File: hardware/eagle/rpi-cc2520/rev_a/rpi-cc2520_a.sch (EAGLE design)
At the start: 11 parts, among them J1 PINHD-2X12/SMD, J2 PINHD-2X12/SMD

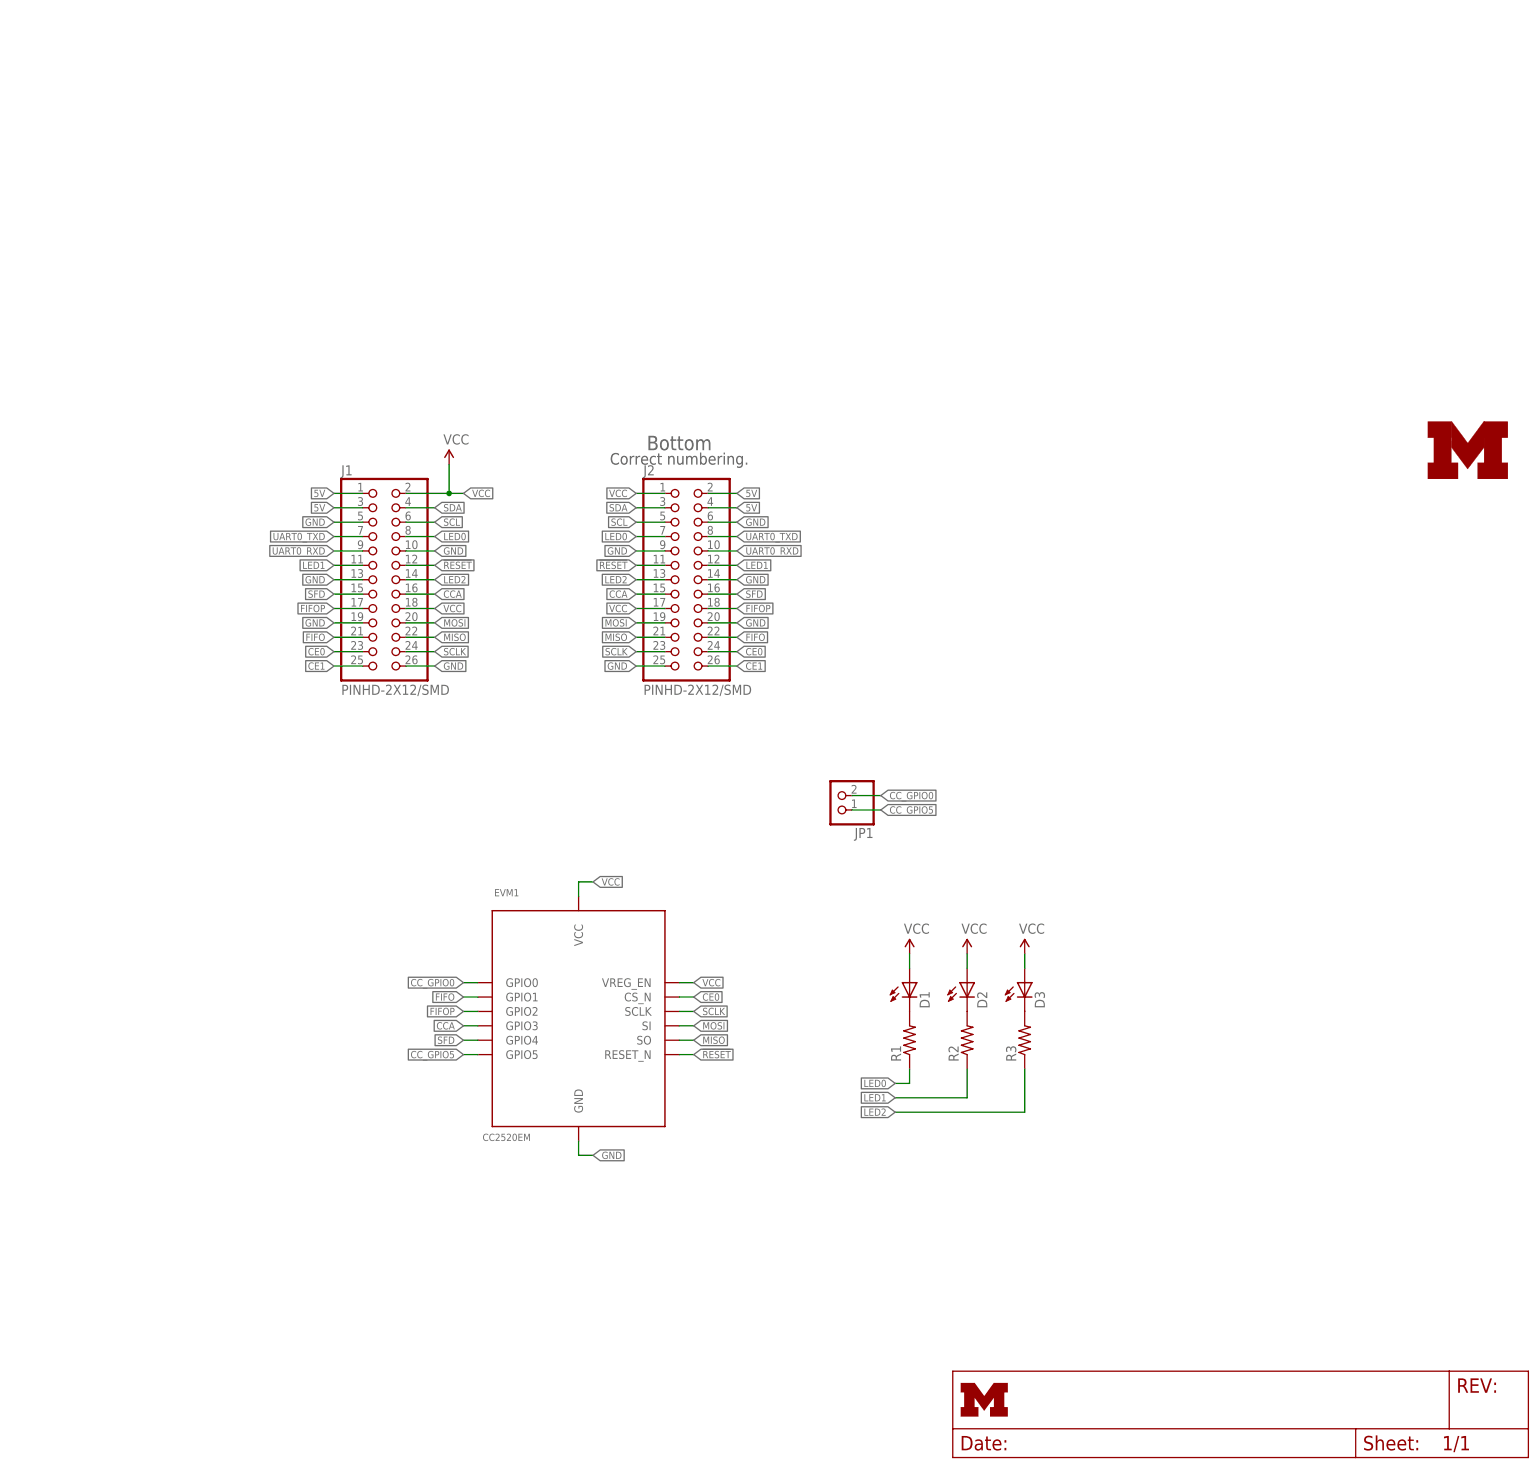
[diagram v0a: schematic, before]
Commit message: adding cc2520 and related parts
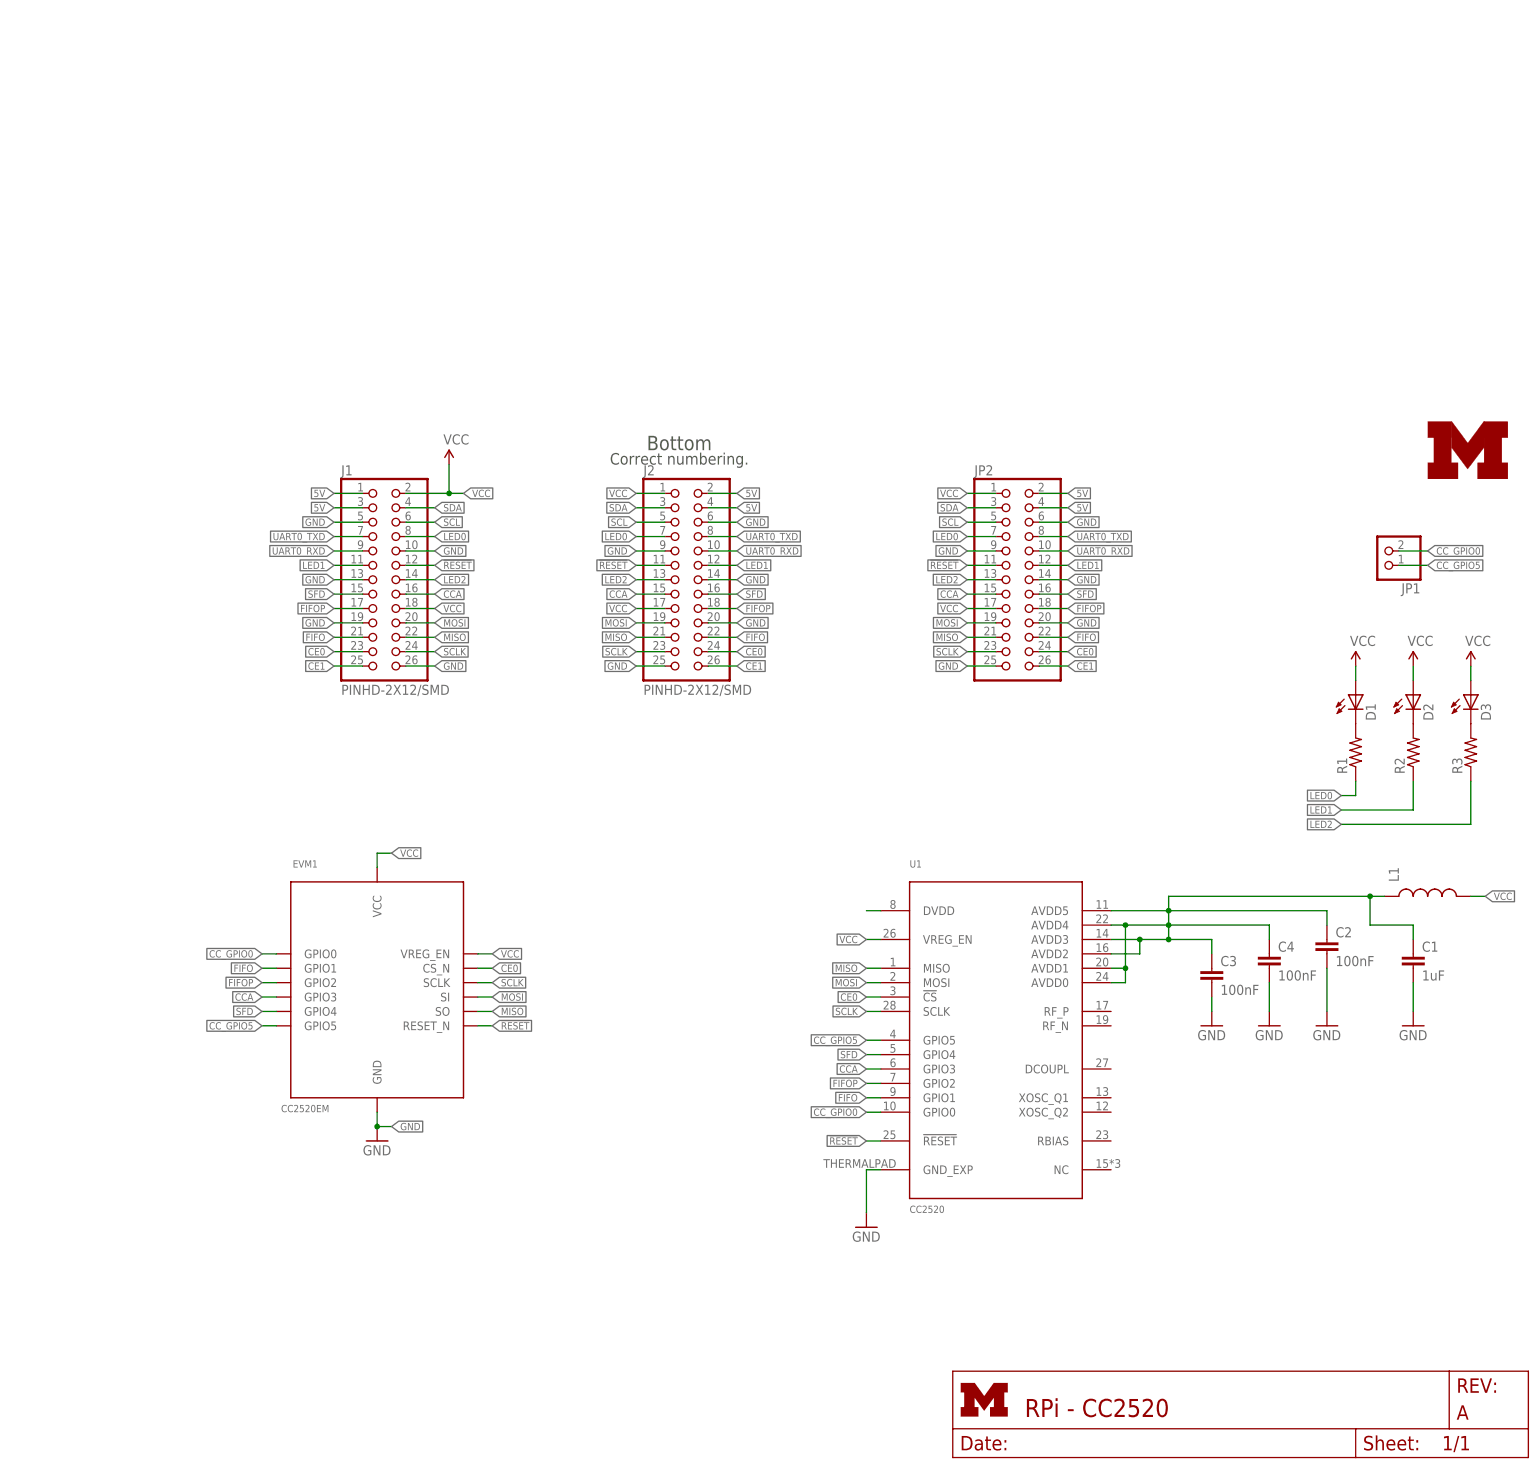
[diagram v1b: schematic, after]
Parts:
- added C1: 1uF, rcl:C-EUC0603
- added C2, C3, C4: 100nF, rcl:C-EUC0402
- added JP2: (no value), pinhead:PINHD-2X13
- added L1: (no value), SparkFun-Passives:INDUCTOR0603
- added U1: CC2520, chips:CC2520
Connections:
- new net N$4: C1.1, C2.1, C3.1, C4.1, L1.1, U1.AVDD0, U1.AVDD1, U1.AVDD2, U1.AVDD3, U1.AVDD4, U1.AVDD5
- new net N$5: U1.DVDD
- net !RESET: now also JP2.11, U1.!RESET
- net 5V: now also JP2.2, JP2.4
- net CCA: now also JP2.15, U1.GPIO3
- net CC_GPIO0: now also U1.GPIO0
- net CC_GPIO5: now also U1.GPIO5
- net CE0: now also JP2.24, U1.!CS
- net CE1: now also JP2.26
- net FIFO: now also JP2.22, U1.GPIO1
- net FIFOP: now also JP2.18, U1.GPIO2
- net GND: now also C1.2, C2.2, C3.2, C4.2, JP2.14, JP2.20, JP2.25, JP2.6, JP2.9, U1.GND_EXP
- net LED0: now also JP2.7
- net LED1: now also JP2.12
- net LED2: now also JP2.13
- net MISO: now also JP2.21, U1.MISO
- net MOSI: now also JP2.19, U1.MOSI
- net SCL: now also JP2.5
- net SCLK: now also JP2.23, U1.SCLK
- net SDA: now also JP2.3
- net SFD: now also JP2.16, U1.GPIO4
- net UART0_RXD: now also JP2.10
- net UART0_TXD: now also JP2.8
- net VCC: now also JP2.1, JP2.17, L1.2, U1.VREG_EN
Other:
- moved on the sheet: D1, D2, D3, EVM1, JP1, R1, R2, R3

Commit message: working on rf path
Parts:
- removed C2, C3, C4: 100nF, rcl:C-EUC0402
- added C141, C151, C161: 100nF, rcl:C-EUC0402
- added C171: 39pF, rcl:C-EUC0402
- added C172: 1.8pF, rcl:C-EUC0402
- added C191: 82pF, rcl:C-EUC0402
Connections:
- new net N$6: C191.2, U1.RF_N
- new net N$7: C171.2, C172.1
- net GND: now also C141.2, C151.2, C161.2; no longer C2.2, C3.2, C4.2
- net N$4: now also C171.1, U1.RF_P; no longer C1.1, C2.1, C3.1, C4.1, L1.1, U1.AVDD0, U1.AVDD1, U1.AVDD2, U1.AVDD3, U1.AVDD4, U1.AVDD5
- net N$5: now also C1.1, C141.1, C151.1, C161.1, L1.1, U1.AVDD0, U1.AVDD1, U1.AVDD2, U1.AVDD3, U1.AVDD4, U1.AVDD5
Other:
- moved on the sheet: C1, EVM1, J1, J2, JP2, L1, U1

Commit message: laying out board
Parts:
- removed EVM1: CC2520EM, brouter:CC2520EM
- removed J1, J2: PINHD-2X12/SMD, headers:PINHD-2X12/SMD
- added C121, C131: 27pF, rcl:C-EUC0402
- added C173: 1.8pF, rcl:C-EUC0402
- added C174: 1pF, rcl:C-EUC0402
- added C192: 1.5pF, rcl:C-EUC0402
- added C271: 100nF, rcl:C-EUC0402
- added P1: MOLEX_73251-135X, connector:MOLEX_73251-135X
- added R231: 56k 1%, rcl:R-US_R0402
- added R4: 1M 1%, rcl:R-US_R0402
- added X1: NX2520SA, rpi-cc2520:NX2520SA
- JP2: DIGIKEY (none) -> SAM1204-13-ND
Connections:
- new net N$10: C174.2, P1.P$1
- new net N$11: C131.1, U1.XOSC_Q1, X1.1
- new net N$12: C271.1, U1.DCOUPL
- new net N$13: C121.1, U1.XOSC_Q2, X1.2
- new net N$14: R231.2, U1.RBIAS
- new net N$8: C191.1, C192.2
- new net N$9: C173.2, C192.1
- net !RESET: no longer EVM1.RESET_N, J1.12, J2.11
- net 5V: no longer J1.1, J1.3, J2.2, J2.4
- net CCA: no longer EVM1.GPIO3, J1.16, J2.15
- net CC_GPIO0: no longer EVM1.GPIO0
- net CC_GPIO5: no longer EVM1.GPIO5
- net CE0: no longer EVM1.CS_N, J1.23, J2.24
- net CE1: no longer J1.25, J2.26
- net FIFO: no longer EVM1.GPIO1, J1.21, J2.22
- net FIFOP: no longer EVM1.GPIO2, J1.17, J2.18
- net GND: now also C121.2, C131.2, C172.2, C173.1, C174.1, C271.2, P1.P$2, P1.P$3, P1.P$4, P1.P$5, R231.1, R4.1; no longer EVM1.GND, J1.10, J1.13, J1.19, J1.26, J1.5, J2.14, J2.20, J2.25, J2.6, J2.9
- net LED0: no longer J1.8, J2.7
- net LED1: no longer J1.11, J2.12
- net LED2: no longer J1.14, J2.13
- net MISO: now also R4.2; no longer EVM1.SO, J1.22, J2.21
- net MOSI: no longer EVM1.SI, J1.20, J2.19
- net SCL: no longer J1.6, J2.5
- net SCLK: no longer EVM1.SCLK, J1.24, J2.23
- net SDA: no longer J1.4, J2.3
- net SFD: no longer EVM1.GPIO4, J1.15, J2.16
- net UART0_RXD: no longer J1.9, J2.10
- net UART0_TXD: no longer J1.7, J2.8
- net VCC: no longer EVM1.VCC, EVM1.VREG_EN, J1.18, J1.2, J2.1, J2.17
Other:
- note removed: "Bottom"
- note removed: "Correct numbering."
- moved on the sheet: C1, C141, C151, C161, C171, C172, L1

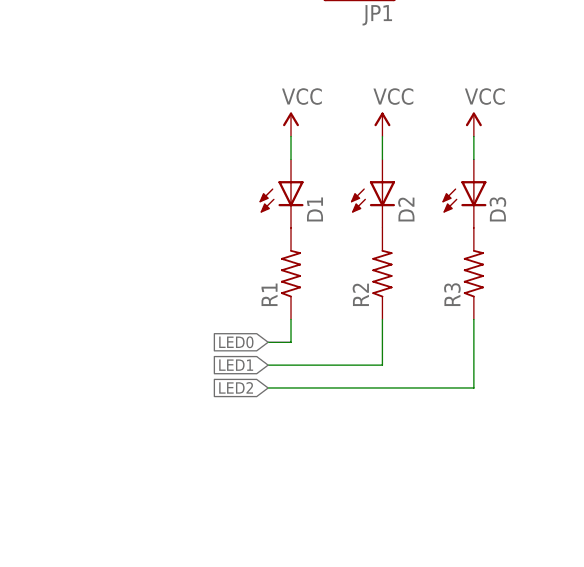
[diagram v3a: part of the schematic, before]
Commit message: updated bom with digikey part numbers
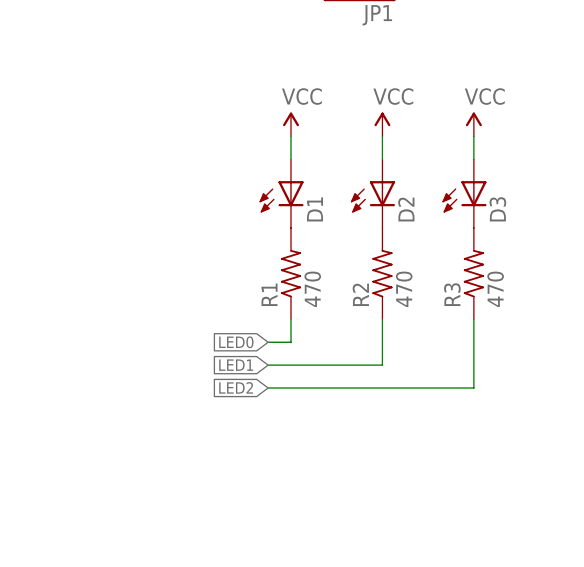
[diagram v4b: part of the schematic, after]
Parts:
- D1: DIGIKEY (none) -> 160-1834-1-ND
- D2: DIGIKEY (none) -> 160-1835-1-ND
- D3: DIGIKEY (none) -> 160-1837-1-ND
- R1, R2, R3: value (none) -> 470
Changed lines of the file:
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@@
 <setting verticaltext="up"/>
 </settings>
-<grid distance="0.1" unitdist="inch" unit="inch" style="lines" multiple="1" display="yes" altdistance="0.01" altunitdist="inch" altunit="inch"/>
+<grid distance="0.1" unitdist="inch" unit="inch" style="lines" multiple="1" display="no" altdistance="0.01" altunitdist="inch" altunit="inch"/>
 <layers>
 <layer number="1" name="Top" color="4" fill="1" visible="no" active="no"/>
@@
 <part name="U$1" library="logos" deviceset="UMICH_SOLID" device="_SMALL"/>
 <part name="JP1" library="pinhead" deviceset="PINHD-1X2" device=""/>
-<part name="D1" library="SparkFun-LED" deviceset="LED" device="0603"/>
-<part name="D2" library="SparkFun-LED" deviceset="LED" device="0603"/>
-<part name="D3" library="SparkFun-LED" deviceset="LED" device="0603"/>
-<part name="R1" library="rcl" deviceset="R-US_" device="R0603"/>
-<part name="R2" library="rcl" deviceset="R-US_" device="R0603"/>
-<part name="R3" library="rcl" deviceset="R-US_" device="R0603"/>
+<part name="D1" library="SparkFun-LED" deviceset="LED" device="0603">
+<attribute name="DIGIKEY" value="160-1834-1-ND"/>
+</part>
+<part name="D2" library="SparkFun-LED" deviceset="LED" device="0603">
+<attribute name="DIGIKEY" value="160-1835-1-ND"/>
+</part>
+<part name="D3" library="SparkFun-LED" deviceset="LED" device="0603">
+<attribute name="DIGIKEY" value="160-1837-1-ND"/>
+</part>
+<part name="R1" library="rcl" deviceset="R-US_" device="R0603" value="470"/>
+<part name="R2" library="rcl" deviceset="R-US_" device="R0603" value="470"/>
+<part name="R3" library="rcl" deviceset="R-US_" device="R0603" value="470"/>
 <part name="P+1" library="SparkFun" deviceset="VCC" device=""/>
 <part name="P+2" library="SparkFun" deviceset="VCC" device=""/>
@@
 <instance part="U$1" gate="G$1" x="231.14" y="172.72"/>
 <instance part="JP1" gate="G$1" x="223.52" y="160.02" rot="R180"/>
-<instance part="D1" gate="G$1" x="218.44" y="134.62"/>
-<instance part="D2" gate="G$1" x="228.6" y="134.62"/>
-<instance part="D3" gate="G$1" x="238.76" y="134.62"/>
+<instance part="D1" gate="G$1" x="218.44" y="134.62">
+<attribute name="DIGIKEY" x="218.44" y="134.62" size="1.27" layer="96" display="off"/>
+</instance>
+<instance part="D2" gate="G$1" x="228.6" y="134.62">
+<attribute name="DIGIKEY" x="228.6" y="134.62" size="1.27" layer="96" display="off"/>
+</instance>
+<instance part="D3" gate="G$1" x="238.76" y="134.62">
+<attribute name="DIGIKEY" x="238.76" y="134.62" size="1.27" layer="96" display="off"/>
+</instance>
 <instance part="R1" gate="G$1" x="218.44" y="124.46" rot="R90"/>
 <instance part="R2" gate="G$1" x="228.6" y="124.46" rot="R90"/>
